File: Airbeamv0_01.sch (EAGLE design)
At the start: 92 parts

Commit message: Fixed Switch issue, updating voltage choosing issue
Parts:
- removed U_ONOFF: PUSHBUTTON, Airbeam:PUSHBUTTON
- added U$3: PUSHBUTTON, Airbeam:PUSHBUTTON
- added VDETECT1: VDETEC_APX, Airbeam:VDETEC_APX
- added VR_MOS-P2: MOSFET-P, Airbeam:MOSFET-P
- VR_R3: value DNP -> 10k; PARTNO RC0603JR-070RL -> RC0603JR-0710KL
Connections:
- new net N$15: VDETECT1.RESET, VR_MOS-P2.P$1
- new net VUSB_G2.9: VR_D1.P$1, VR_MOS-P1.P$1, VR_MOS-P2.P$2, VR_R1.1
- net GND: now also VDETECT1.GND
- net N$5: no longer VR_R3.2
- net UGND: now also VR_R3.1
- net VDETECT_VDD: now also U$3.LS1, U$3.LS2; no longer U_ONOFF.COM1, U_ONOFF.COM2
- net VREG_IN: now also U$3.COM1, U$3.COM2; no longer U_ONOFF.P1, U_ONOFF.P2, U_ONOFF.P3, U_ONOFF.P4
- net VUSB: now also VDETECT1.VDD, VR_MOS-P2.P$3, VR_R3.2; no longer VR_D1.P$1, VR_MOS-P1.P$1, VR_R1.1
- net V_BAT: no longer VR_R3.1
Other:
- note added: "TODO: - Make U_ILIM wider - Put metal on switch mounting holes - Power switch has incorrect circuit diagram, fix - Voltage output is 5.1V -- check out why - Move Buffer away from BT module - Make dust connector holes slightly larger"
- note removed: "TODO:"
- moved on the sheet: VR_R3

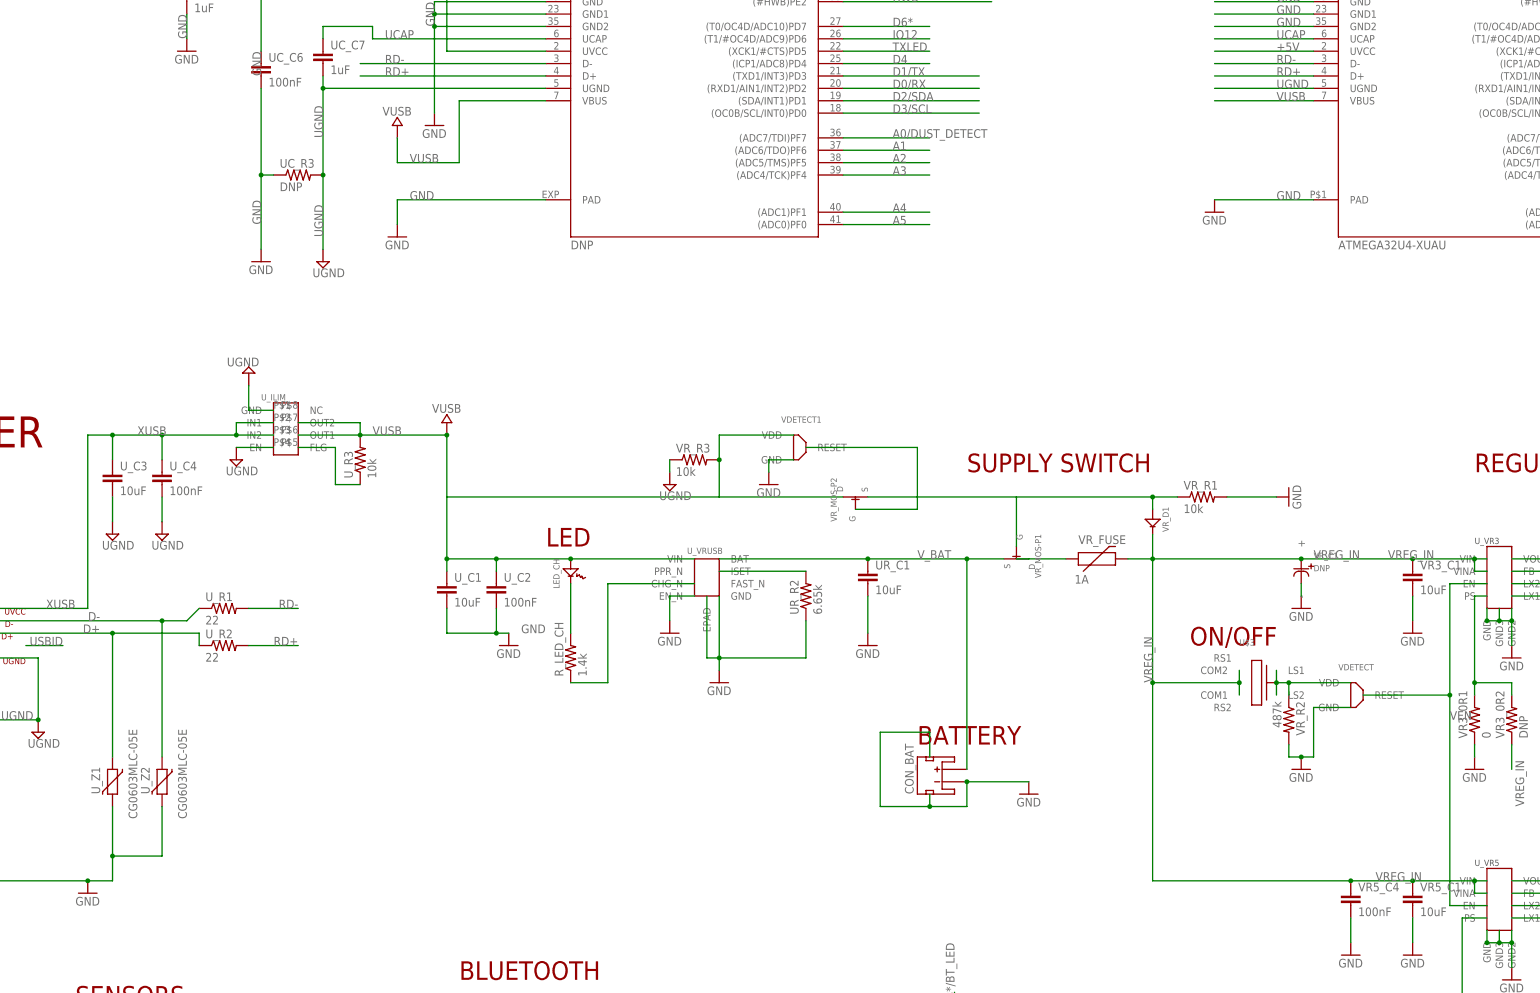
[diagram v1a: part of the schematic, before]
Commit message: removed most usb + battery chips and replaced with single chip
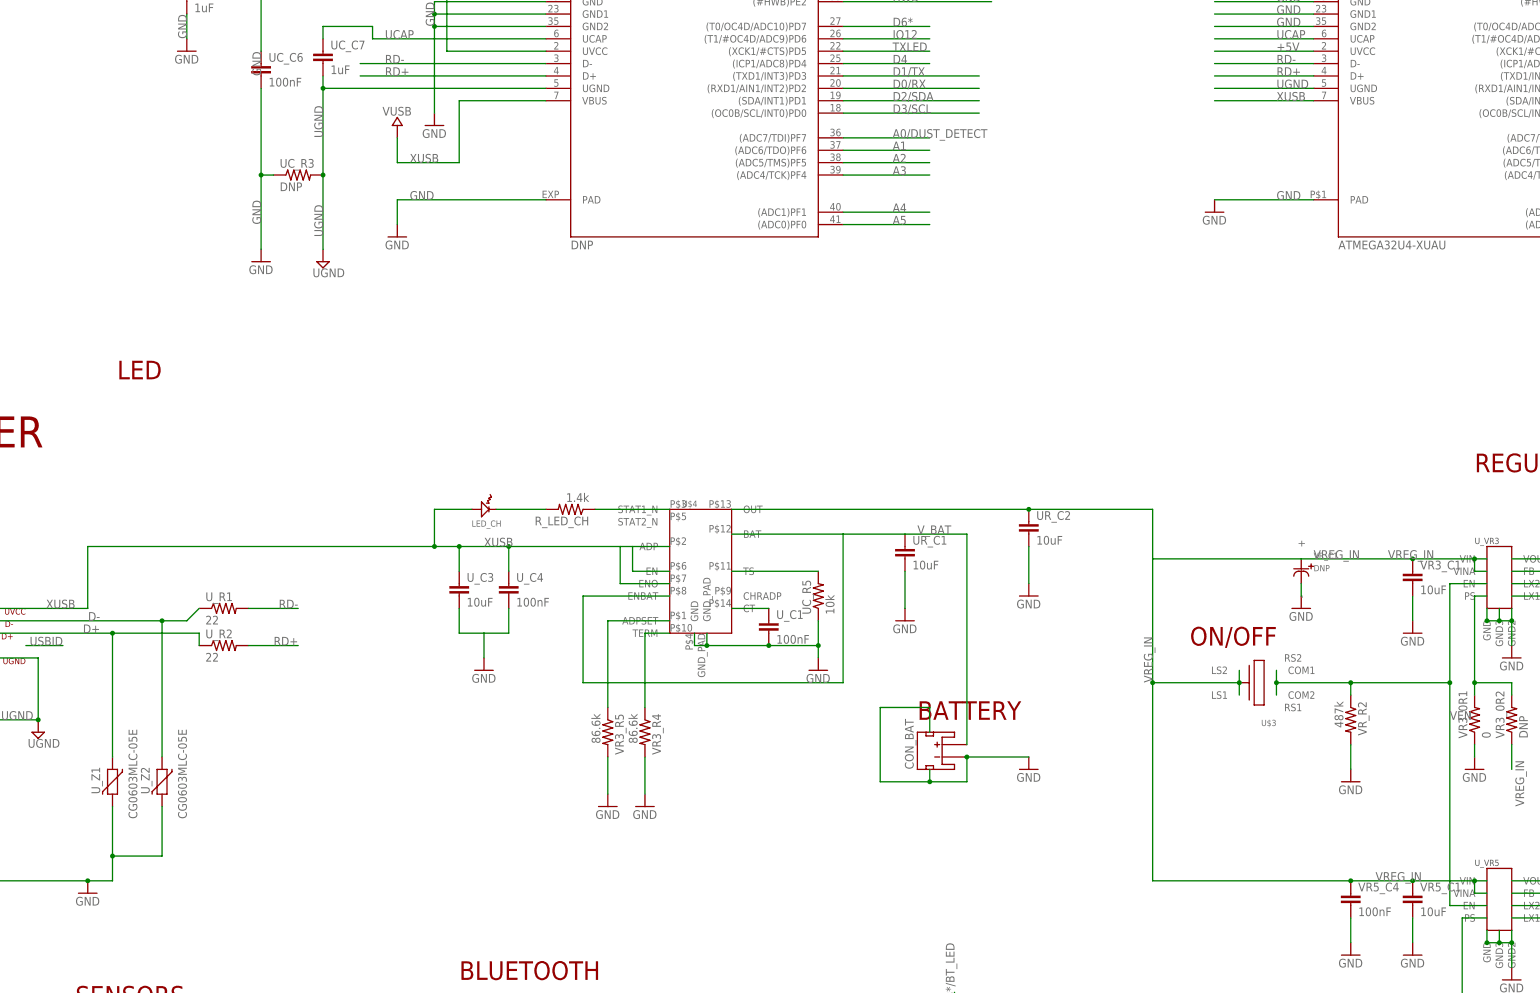
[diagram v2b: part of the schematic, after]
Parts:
- removed UR_R2: 6.65k, SparkFun-Passives:RESISTOR0603-RES
- removed U_C2: 100nF, SparkFun-Passives:CAP0603-CAP
- removed U_ILIM: USB-OVERCURRENT, Airbeam:USB-OVERCURRENT
- removed U_R3: 10k, SparkFun-Passives:RESISTOR0603-RES
- removed U_VRUSB: VREG_MC34673, Airbeam:VREG_MC34673
- removed VDETECT, VDETECT1: VDETEC_APX, Airbeam:VDETEC_APX
- removed VR_D1: DIODESOD123, Airbeam:DIODESOD123
- removed VR_FUSE: 1A, SparkFun-PowerIC:PTCSMD-W
- removed VR_MOS-P1, VR_MOS-P2: MOSFET-P, Airbeam:MOSFET-P
- removed VR_R1, VR_R3: 10k, SparkFun-Resistors:RESISTOR0603
- added U$4: USB-BATTERY_LOAD, Airbeam:USB-BATTERY_LOAD
- added UC_R5: 10k, SparkFun-Passives:RESISTOR0603-RES
- added UR_C2: 10uF, SparkFun-Passives:CAP0805
- added VR3_R4, VR3_R5: 86.6k, SparkFun-Resistors:RESISTOR0603
- U_C1: value 10uF -> 100nF; device SparkFun-Passives:CAP0805 -> SparkFun-Passives:CAP0603-CAP; PARTNO C2012X5R1C106K085AC -> C1608X7R1E104K080AA
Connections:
- removed net N$13: R_LED_CH.1, U_VRUSB.CHG_N
- removed net N$16: UR_R2.2, U_VRUSB.ISET
- removed net VDETECT_VDD: U$3.LS1, U$3.LS2, VDETECT.VDD, VR_R2.1
- removed net VUSB: ATMEGA32U4-T.VBUS, LED_CH.AN, U_C1.1, U_C2.1, U_ILIM.OUT1, U_ILIM.OUT2, U_MEGA32U-Q.VBUS, U_R3.2, U_VRUSB.VIN, VDETECT1.VDD, VR_MOS-P2.P$3, VR_R3.2
- removed net VUSB_G2.9: VR_D1.P$1, VR_MOS-P1.P$1, VR_MOS-P2.P$2, VR_R1.1
- new net N$2: U$4.TERM, VR3_R4.1
- new net N$6: U$4.CT, U_C1.1
- net GND: now also U$4.GND, U$4.GND_PAD, UC_R5.1, UR_C2.2, U_C3.2, U_C4.2, VR3_R4.2, VR3_R5.2; no longer UR_R2.1, U_C2.2, U_VRUSB.EN_N, U_VRUSB.EPAD, U_VRUSB.GND, VDETECT.GND, VDETECT1.GND, VR_R1.2
- net N$15: now also U$4.ADPSET, VR3_R5.1; no longer VDETECT1.RESET, VR_MOS-P2.P$1
- net N$5: now also U$4.TS, UC_R5.2; no longer VR_FUSE.1, VR_MOS-P1.P$3
- net N$8: now also R_LED_CH.1, U$4.STAT1_N; no longer U_ILIM.FLG, U_R3.1
- net UGND: no longer U_C3.2, U_C4.2, U_ILIM.EN, U_ILIM.GND, VR_R3.1
- net VEN: now also U$3.COM1, U$3.COM2, VR_R2.1; no longer VDETECT.RESET
- net VREG_IN: now also U$3.LS1, U$3.LS2, U$4.OUT, UR_C2.1; no longer U$3.COM1, U$3.COM2, VR_D1.P$2, VR_FUSE.2
- net V_BAT: now also U$4.BAT, U$4.ENBAT; no longer U_VRUSB.BAT, VR_MOS-P1.P$2
- net XUSB: now also ATMEGA32U4-T.VBUS, LED_CH.AN, U$4.ADP, U$4.EN, U$4.ENO, U_MEGA32U-Q.VBUS; no longer U_ILIM.IN1, U_ILIM.IN2
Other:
- note removed: "SUPPLY SWITCH"
- moved on the sheet: CON_BAT, LED_CH, R_LED_CH, U$3, UR_C1, U_C1, U_C3, U_C4, VR_R2

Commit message: updated according to Daves suggestions
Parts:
- removed CON_ADDON: CON_1X52MM, Airbeam:CON_1X52MM
- removed UC_R5: 10k, SparkFun-Passives:RESISTOR0603-RES
- added CTH_R1, UC_R6: 10k, SparkFun-Passives:RESISTOR0603-RES
- added UC_NTC: 10k, Airbeam:THERMISTOR0402
- added U_USB_CH: USB-BATTERY_LOAD, Airbeam:USB-BATTERY_LOAD
- U$4: value USB-BATTERY_LOAD -> TBLOCK_5; device Airbeam:USB-BATTERY_LOAD -> Airbeam:TBLOCK_5
- U_C3: value 10uF -> 10uF/50V; device SparkFun-Passives:CAP0805 -> SparkFun-Passives:CAP1206; PARTNO C2012X5R1C106K085AC -> CL31A106KBHNNNE
- U_C4: PARTNO C1608X7R1E104K080AA -> CC0603ZRY5V9BB104
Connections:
- net +3V3: now also U$4.B_3, U$4.T_3; no longer CON_ADDON.P$3
- net +5V: now also CTH_R1.1, U$4.B_4, U$4.T_4; no longer CON_ADDON.P$4
- net A1: now also U$4.B_1, U$4.T_1; no longer CON_ADDON.P$1
- net A2: now also U$4.B_2, U$4.T_2; no longer CON_ADDON.P$2
- net GND: now also UC_NTC.P$1, U_USB_CH.GND, U_USB_CH.GND_PAD; no longer U$4.GND, U$4.GND_PAD, UC_R5.1
- net IO9*/TH_DETECT: now also CTH_R1.2
- net N$15: now also U_USB_CH.ADPSET; no longer U$4.ADPSET
- net N$2: now also U_USB_CH.TERM; no longer U$4.TERM
- net N$5: now also UC_NTC.P$2, UC_R6.1, U_USB_CH.TS; no longer U$4.TS, UC_R5.2
- net N$6: now also U_USB_CH.CT; no longer U$4.CT
- net N$7: now also U$4.B_5, U$4.T_5; no longer CON_ADDON.P$5
- net N$8: now also U_USB_CH.STAT1_N; no longer U$4.STAT1_N
- net VREG_IN: now also U_USB_CH.OUT; no longer U$4.OUT
- net V_BAT: now also U_USB_CH.BAT, U_USB_CH.ENBAT; no longer U$4.BAT, U$4.ENBAT
- net XUSB: now also UC_R6.2, U_USB_CH.ADP, U_USB_CH.EN, U_USB_CH.ENO; no longer U$4.ADP, U$4.EN, U$4.ENO
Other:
- note added: "TODO: - X Make U_ILIM wider - X Put metal on switch mounting holes - X Power switch has incorrect circuit diagram, fix - X Voltage output is 5.1V -- check out why - X Move Buffer away from BT module - Make dust connector holes slightly larger - Flip T+RH Sensor Connections"
- note removed: "TODO: - Make U_ILIM wider - Put metal on switch mounting holes - Power switch has incorrect circuit diagram, fix - Voltage output is 5.1V -- check out why - Move Buffer away from BT module - Make dust connector holes slightly larger"
- moved on the sheet: CTH_C1, LED_CH, R_LED_CH, U_C3, U_C4, U_TEMP-HUM

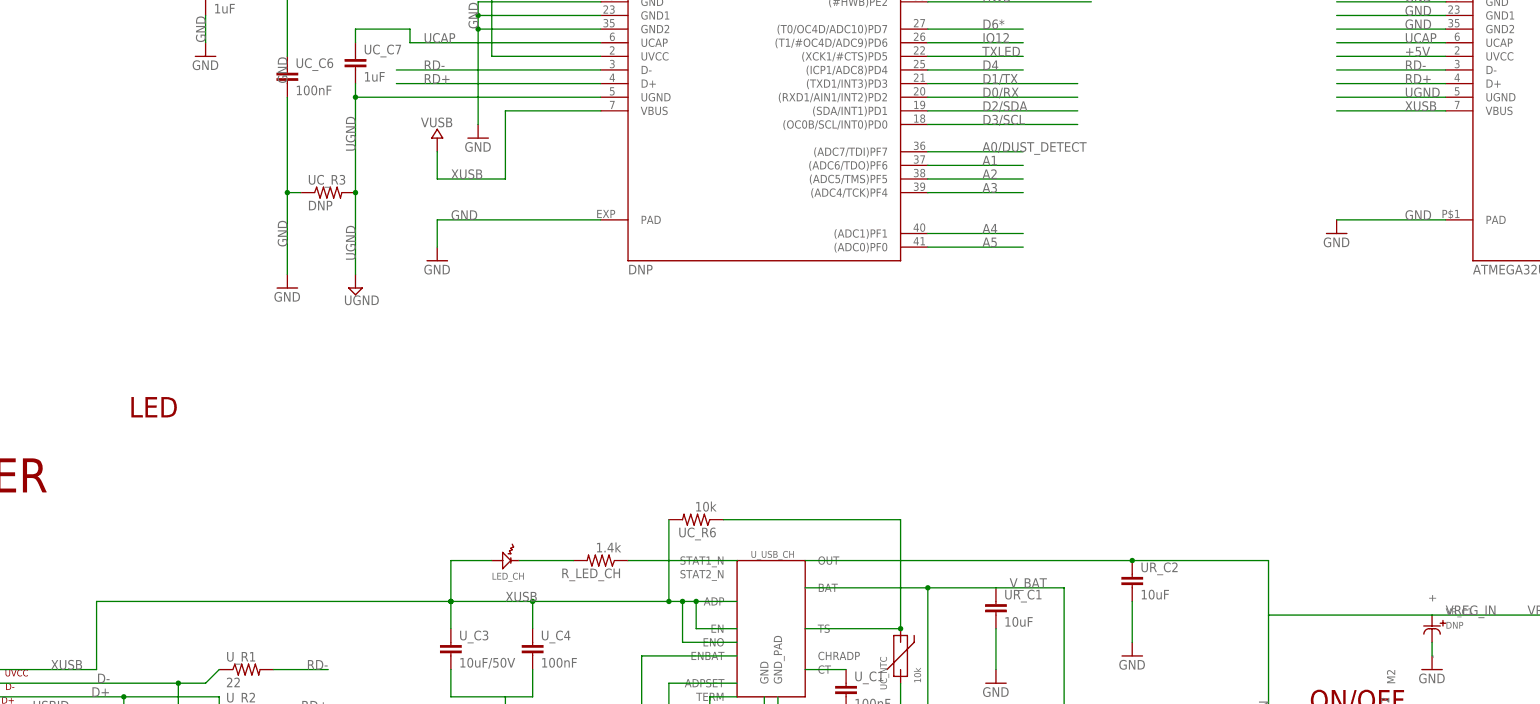
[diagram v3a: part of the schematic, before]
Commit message: updated bom, added ferrite bead
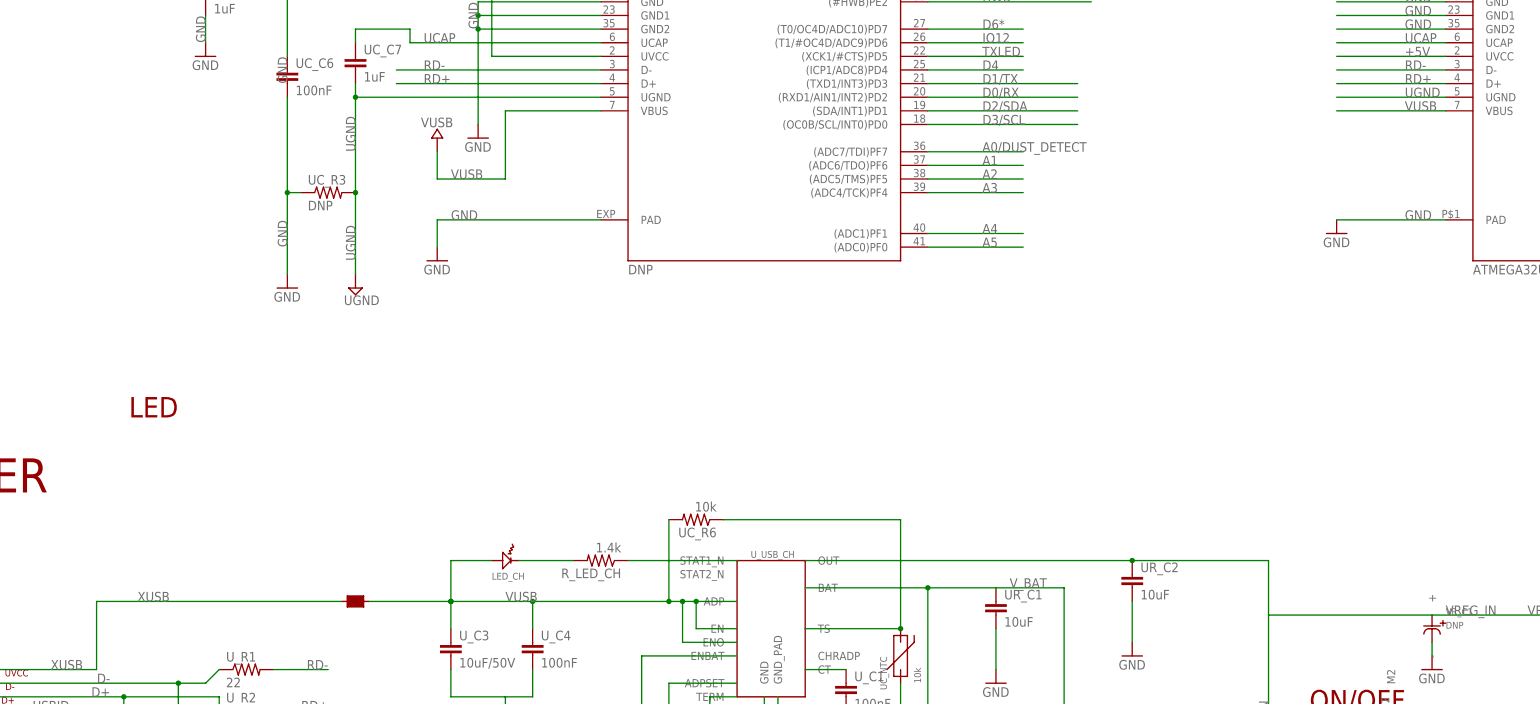
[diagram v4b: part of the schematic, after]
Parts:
- added U_FB3: FERITE_BEAD, Airbeam:FERITE_BEAD
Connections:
- new net VUSB: ATMEGA32U4-T.VBUS, LED_CH.AN, UC_R6.2, U_C3.1, U_C4.1, U_FB3.P$2, U_MEGA32U-Q.VBUS, U_USB_CH.ADP, U_USB_CH.EN, U_USB_CH.ENO
- net XUSB: now also U_FB3.P$1; no longer ATMEGA32U4-T.VBUS, LED_CH.AN, UC_R6.2, U_C3.1, U_C4.1, U_MEGA32U-Q.VBUS, U_USB_CH.ADP, U_USB_CH.EN, U_USB_CH.ENO
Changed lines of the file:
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@@
 <schematic xreflabel="%F%N/%S.%C%R" xrefpart="/%S.%C%R">
 <attributes>
+<attribute name="DATABASE" value="./BOM/Airbeam-PARTSDB.csv"/>
 </attributes>
 <variantdefs>
@@
 <parts>
 <part name="CON_ICSP" library="SmartPrj" deviceset="PINHD-2X3" device="" value="ICSP">
+<attribute name="DNP" value=""/>
 <attribute name="PARTNO" value="67997-206HLF "/>
 </part>
@@
 </part>
 <part name="VR3_0R2" library="SparkFun-Passives" deviceset="RESISTOR" device="0603-RES" value="DNP">
+<attribute name="DNP" value=""/>
 <attribute name="PARTNO" value="RC0603JR-070RL"/>
 </part>
 <part name="GND37" library="supply1" deviceset="GND" device=""/>
 <part name="VR5_0R1" library="SparkFun-Passives" deviceset="RESISTOR" device="0603-RES" value="DNP">
+<attribute name="DNP" value=""/>
 <attribute name="PARTNO" value="RC0603JR-070RL"/>
 </part>
@@
 <part name="GND21" library="supply1" deviceset="GND" device=""/>
 <part name="GND38" library="supply1" deviceset="GND" device=""/>
-<part name="RESET_SWITCH" library="Airbeam" deviceset="SWITCH" device=""/>
+<part name="RESET_SWITCH" library="Airbeam" deviceset="SWITCH" device="">
+<attribute name="DNP" value=""/>
+</part>
 <part name="U_Z3" library="varistor" deviceset="VARISTOR" device="CN0603" value="CG0603MLC-05E">
 <attribute name="PARTNO" value="CG0603MLC-05E"/>
@@
 <attribute name="PARTNO" value="MH2029-600Y"/>
 </part>
-<part name="U$1" library="Airbeam" deviceset="MOSFET-N" device=""/>
+<part name="U$1" library="Airbeam" deviceset="MOSFET-N" device="">
+<attribute name="DNP" value=""/>
+</part>
 <part name="U_C4" library="SparkFun-Passives" deviceset="CAP" device="0603-CAP" value="100nF">
 <attribute name="PARTNO" value="CC0603ZRY5V9BB104"/>
@@
 </part>
 <part name="U$4" library="Airbeam" deviceset="TBLOCK_5" device=""/>
+<part name="U_FB3" library="Airbeam" deviceset="FERITE_BEAD" device="">
+<attribute name="PARTNO" value="MH2029-600Y"/>
+</part>
 </parts>
 <sheets>
@@
 <attribute name="VALUE" x="-54.61" y="170.18" size="1.778" layer="96"/>
 <attribute name="PARTNO" x="-58.42" y="165.1" size="1.778" layer="96" display="off"/>
+<attribute name="DNP" x="-58.42" y="165.1" size="1.778" layer="96" display="off"/>
 </instance>
 <instance part="P+1" gate="1" x="-43.18" y="177.8" smashed="yes">
@@
 <instance part="VR3_0R2" gate="G$1" x="190.5" y="-55.88" rot="R90">
 <attribute name="PARTNO" x="190.5" y="-55.88" size="1.778" layer="96" rot="R90" display="off"/>
+<attribute name="DNP" x="190.5" y="-55.88" size="1.778" layer="96" rot="R90" display="off"/>
 </instance>
 <instance part="GND37" gate="1" x="180.34" y="-134.62"/>
 <instance part="VR5_0R1" gate="G$1" x="180.34" y="-121.92" rot="R90">
 <attribute name="PARTNO" x="180.34" y="-121.92" size="1.778" layer="96" rot="R90" display="off"/>
+<attribute name="DNP" x="180.34" y="-121.92" size="1.778" layer="96" rot="R90" display="off"/>
 </instance>
 <instance part="VR5_0R2" gate="G$1" x="187.96" y="-121.92" rot="R90">
@@
 <instance part="GND21" gate="1" x="190.5" y="-43.18"/>
 <instance part="GND38" gate="1" x="190.5" y="-109.22"/>
-<instance part="RESET_SWITCH" gate="G$1" x="-104.14" y="170.18"/>
+<instance part="RESET_SWITCH" gate="G$1" x="-104.14" y="170.18">
+<attribute name="DNP" x="-104.14" y="170.18" size="1.778" layer="96" display="off"/>
+</instance>
 <instance part="U_Z3" gate="G$1" x="-149.86" y="-167.64" smashed="yes">
 <attribute name="NAME" x="-152.4" y="-165.1" size="1.778" layer="95"/>
@@
 <attribute name="PARTNO" x="-50.8" y="104.14" size="1.778" layer="96" rot="R90" display="off"/>
 </instance>
-<instance part="U$1" gate="G$1" x="-96.52" y="-162.56" rot="R270"/>
+<instance part="U$1" gate="G$1" x="-96.52" y="-162.56" rot="R270">
+<attribute name="DNP" x="-96.52" y="-162.56" size="1.778" layer="96" rot="R270" display="off"/>
+</instance>
 <instance part="U_C4" gate="G$1" x="-20.32" y="-30.48">
 <attribute name="PARTNO" x="-20.32" y="-30.48" size="1.778" layer="96" display="off"/>
@@
 </instance>
 <instance part="U$4" gate="G$1" x="-127" y="-154.94"/>
+<instance part="U_FB3" gate="G$1" x="-53.34" y="-20.32" rot="R90">
+<attribute name="PARTNO" x="-53.34" y="-20.32" size="1.778" layer="96" rot="R90" display="off"/>
+</instance>
 </instances>
 <busses>
@@
 </segment>
 </net>
-<net name="XUSB" class="3">
-<segment>
-<wire x1="-101.6" y1="-33.02" x2="-101.6" y2="-20.32" width="0.1524" layer="91"/>
-<wire x1="-101.6" y1="-20.32" x2="-35.56" y2="-20.32" width="0.1524" layer="91"/>
+<net name="VUSB" class="3">
+<segment>
 <wire x1="-35.56" y1="-20.32" x2="-20.32" y2="-20.32" width="0.1524" layer="91"/>
-<wire x1="-121.92" y1="-33.02" x2="-101.6" y2="-33.02" width="0.1524" layer="91"/>
-<label x="-104.14" y="-33.02" size="1.778" layer="95" rot="MR0"/>
 <label x="-25.4" y="-20.32" size="1.778" layer="95"/>
-<pinref part="CON_USB" gate="G$1" pin="T1"/>
 <wire x1="-35.56" y1="-25.4" x2="-35.56" y2="-20.32" width="0.1524" layer="91"/>
 <pinref part="U_C4" gate="G$1" pin="1"/>
@@
 <junction x="5.08" y="-20.32"/>
 <pinref part="U_C3" gate="G$1" pin="1"/>
+<pinref part="U_FB3" gate="G$1" pin="P$2"/>
+<wire x1="-50.8" y1="-20.32" x2="-35.56" y2="-20.32" width="0.1524" layer="91"/>
 </segment>
 <segment>
@@
 </segment>
 </net>
+<net name="XUSB" class="3">
+<segment>
+<pinref part="CON_USB" gate="G$1" pin="T1"/>
+<wire x1="-121.92" y1="-33.02" x2="-101.6" y2="-33.02" width="0.1524" layer="91"/>
+<wire x1="-101.6" y1="-33.02" x2="-101.6" y2="-20.32" width="0.1524" layer="91"/>
+<label x="-104.14" y="-33.02" size="1.778" layer="95" rot="MR0"/>
+<label x="-93.98" y="-20.32" size="1.778" layer="95"/>
+<pinref part="U_FB3" gate="G$1" pin="P$1"/>
+<wire x1="-101.6" y1="-20.32" x2="-55.88" y2="-20.32" width="0.1524" layer="91"/>
+</segment>
+</net>
